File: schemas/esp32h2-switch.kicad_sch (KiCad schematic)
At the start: 19 parts, among them J1 Screw_Terminal_01x02, J2 Screw_Terminal_01x02, K1 SPDT, 5V, 10A 250VAC, Q1 NPN, 40V, 500mA, U1 LM1117MP-3.3, U2 ESP32-H2-DEVKITM-1-N4

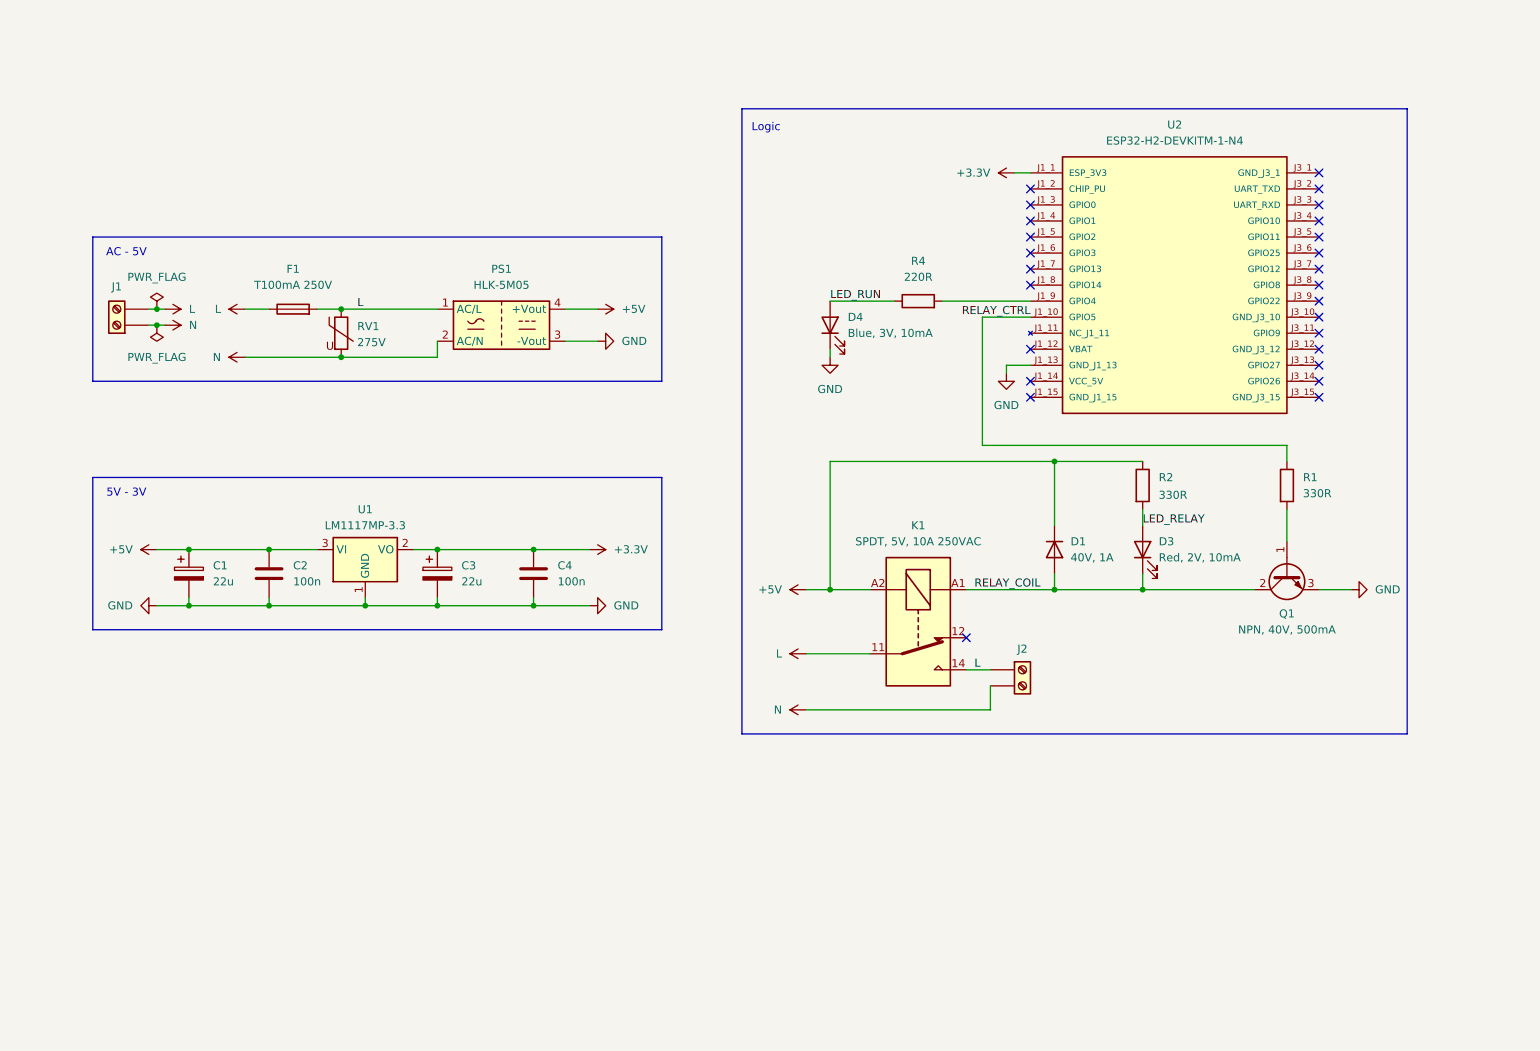
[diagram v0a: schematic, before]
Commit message: Replace devkit on schema with header pings
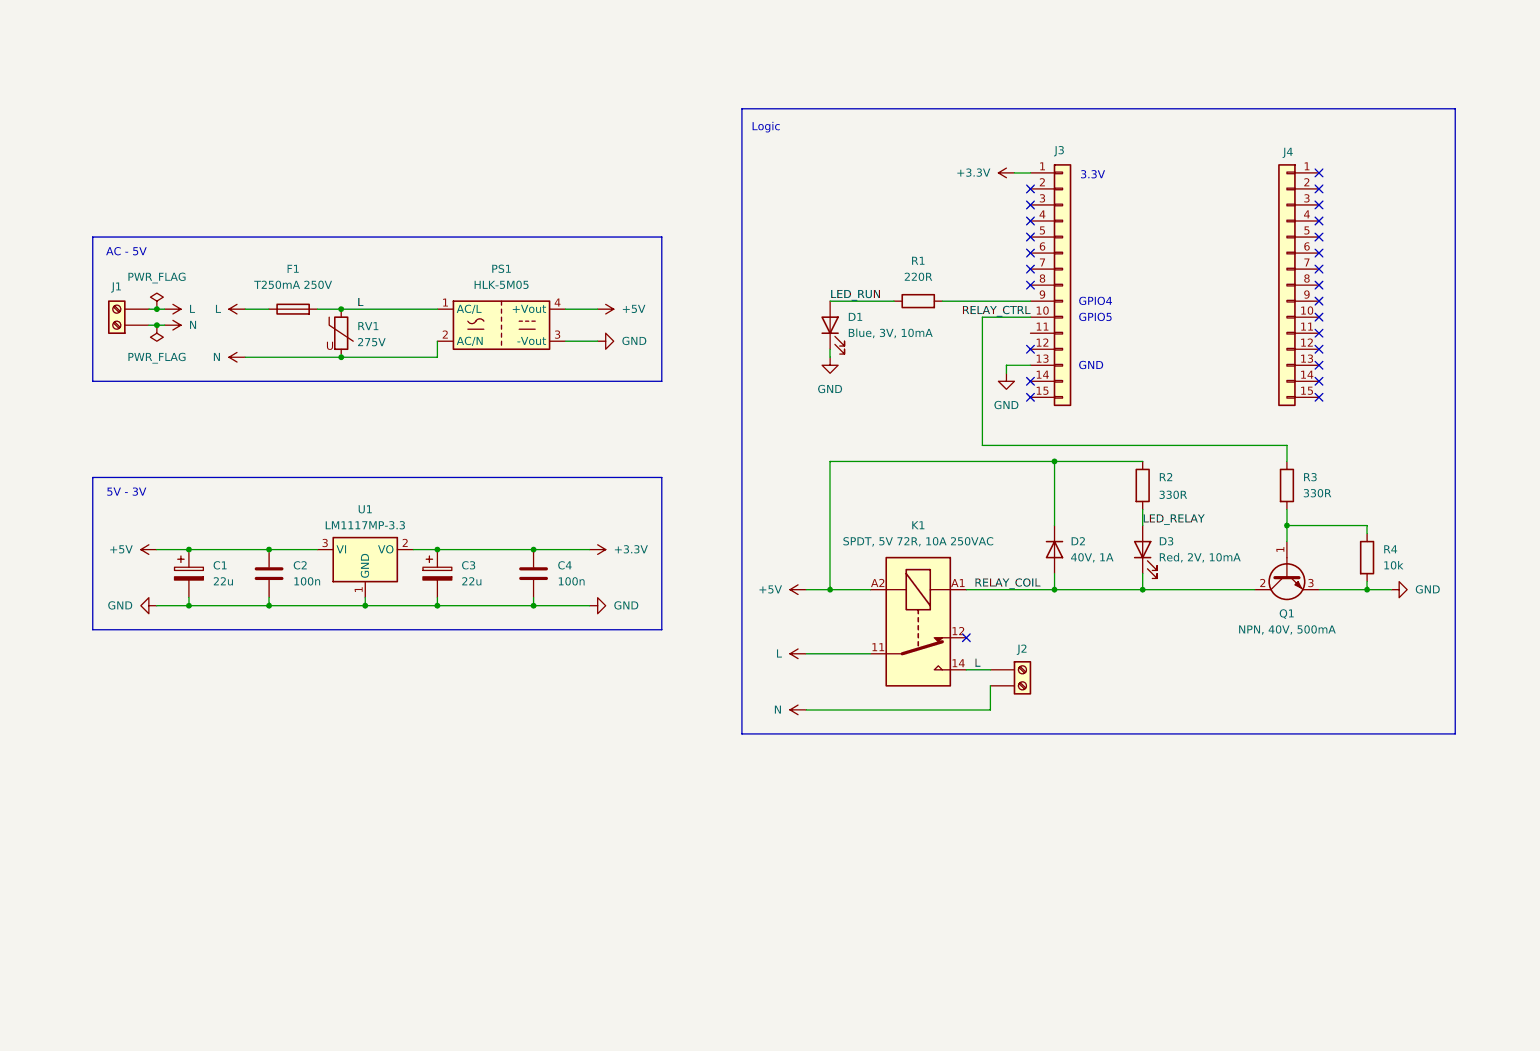
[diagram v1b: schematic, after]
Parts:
- removed U2: ESP32-H2-DEVKITM-1-N4, ESP32-H2-DEVKITM-1-N4:MODULE_ESP32-H2-DEVKITM-1-N4, symbol ESP32-H2-DEVKITM-1-N4:ESP32-H2-DEVKITM-1-N4
- added J3, J4: Conn_01x15, symbol Connector_Generic:Conn_01x15
- added R4: 10k, symbol Device:R
- F1: value T100mA 250V -> T250mA 250V
- K1: value SPDT, 5V, 10A 250VAC -> SPDT, 5V 72R, 10A 250VAC
- renumbered D4 to D1, D1 to D2, R4 to R1, R1 to R3
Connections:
- net +3.3V: now also J3.1 (Pin_1)
- net GND: now also J3.13 (Pin_13), R4.2
- net RELAY_CTRL: now also J3.10 (Pin_10)
- net at Q1.1 (B), R3.2: now also R4.1
- net at R1.2: now also J3.9 (Pin_9)
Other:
- note added: "3.3V"
- note added: "GND"
- note added: "GPIO4"
- note added: "GPIO5"

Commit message: ERC checks
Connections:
- no-connect marks 26 -> 27

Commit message: Add footprints to schematic
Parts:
- C1, C3: footprint (none) -> Sivakov_Capacitors_THT:CP_Radial_D5.0mm_P1.50mm
- C2, C4: footprint (none) -> Capacitor_THT:C_Disc_D5.0mm_W2.5mm_P5.00mm
- D1, D3: footprint (none) -> LED_THT:LED_D3.0mm
- D2: footprint (none) -> Diode_THT:D_DO-41_SOD81_P10.16mm_Horizontal
- F1: footprint (none) -> Sivakov_FuseHolders_THT:FuseHolder_THT_5x20mm_PTF76_RM15mm
- J1, J2: footprint (none) -> TerminalBlock_Phoenix:TerminalBlock_Phoenix_MKDS-1,5-2-5.08_1x02_P5.08mm_Horizontal
- J3, J4: footprint (none) -> Connector_PinSocket_2.54mm:PinSocket_1x15_P2.54mm_Vertical
- K1: footprint (none) -> Sivakov_Relays_THT:Relay_SPDT_Relpol-RM51
- Q1: footprint (none) -> Package_TO_SOT_THT:TO-92_Inline
- R1, R2, R3, R4: footprint (none) -> Resistor_THT:R_Axial_DIN0207_L6.3mm_D2.5mm_P7.62mm_Horizontal
- RV1: footprint (none) -> Varistor:RV_Disc_D9mm_W3.4mm_P5mm
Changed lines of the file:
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@@
 			)
 		)
-		(property "Footprint" ""
+		(property "Footprint" "Package_TO_SOT_THT:TO-92_Inline"
 			(at 231.14 118.11 0)
 			(effects
@@
 			)
 		)
-		(property "Footprint" ""
+		(property "Footprint" "Capacitor_THT:C_Disc_D5.0mm_W2.5mm_P5.00mm"
 			(at 115.2652 116.84 0)
 			(effects
@@
 			)
 		)
-		(property "Footprint" ""
+		(property "Footprint" "TerminalBlock_Phoenix:TerminalBlock_Phoenix_MKDS-1,5-2-5.08_1x02_P5.08mm_Horizontal"
 			(at 191.77 128.27 0)
 			(effects
@@
 			)
 		)
-		(property "Footprint" ""
+		(property "Footprint" "LED_THT:LED_D3.0mm"
 			(at 210.82 109.22 0)
 			(effects
@@
 			)
 		)
-		(property "Footprint" ""
+		(property "Footprint" "Capacitor_THT:C_Disc_D5.0mm_W2.5mm_P5.00mm"
 			(at 73.3552 116.84 0)
 			(effects
@@
 			)
 		)
-		(property "Footprint" ""
+		(property "Footprint" "Diode_THT:D_DO-41_SOD81_P10.16mm_Horizontal"
 			(at 196.85 109.22 0)
 			(effects
@@
 			)
 		)
-		(property "Footprint" ""
+		(property "Footprint" "Resistor_THT:R_Axial_DIN0207_L6.3mm_D2.5mm_P7.62mm_Horizontal"
 			(at 175.26 71.628 90)
 			(effects
@@
 			)
 		)
-		(property "Footprint" ""
+		(property "Footprint" "Sivakov_Relays_THT:Relay_SPDT_Relpol-RM51"
 			(at 173.99 132.08 0)
 			(effects
@@
 			)
 		)
-		(property "Footprint" ""
+		(property "Footprint" "Resistor_THT:R_Axial_DIN0207_L6.3mm_D2.5mm_P7.62mm_Horizontal"
 			(at 209.042 99.06 90)
 			(effects
@@
 			)
 		)
-		(property "Footprint" ""
+		(property "Footprint" "LED_THT:LED_D3.0mm"
 			(at 161.29 73.66 0)
 			(effects
@@
 			)
 		)
-		(property "Footprint" ""
+		(property "Footprint" "Sivakov_Capacitors_THT:CP_Radial_D5.0mm_P1.50mm"
 			(at 100.0252 116.84 0)
 			(effects
@@
 			)
 		)
-		(property "Footprint" ""
+		(property "Footprint" "Varistor:RV_Disc_D9mm_W3.4mm_P5mm"
 			(at 82.042 74.93 90)
 			(effects
@@
 			)
 		)
-		(property "Footprint" ""
+		(property "Footprint" "Sivakov_FuseHolders_THT:FuseHolder_THT_5x20mm_PTF76_RM15mm"
 			(at 76.2 72.898 90)
 			(effects
@@
 			)
 		)
-		(property "Footprint" ""
+		(property "Footprint" "Sivakov_Capacitors_THT:CP_Radial_D5.0mm_P1.50mm"
 			(at 60.6552 116.84 0)
 			(effects
@@
 			)
 		)
-		(property "Footprint" ""
+		(property "Footprint" "Connector_PinSocket_2.54mm:PinSocket_1x15_P2.54mm_Vertical"
 			(at 233.68 67.31 0)
 			(effects
@@
 			)
 		)
-		(property "Footprint" ""
+		(property "Footprint" "TerminalBlock_Phoenix:TerminalBlock_Phoenix_MKDS-1,5-2-5.08_1x02_P5.08mm_Horizontal"
 			(at 48.26 73.66 0)
 			(effects
@@
 			)
 		)
-		(property "Footprint" ""
+		(property "Footprint" "Connector_PinSocket_2.54mm:PinSocket_1x15_P2.54mm_Vertical"
 			(at 198.12 67.31 0)
 			(effects
@@
 			)
 		)
-		(property "Footprint" ""
+		(property "Footprint" "Resistor_THT:R_Axial_DIN0207_L6.3mm_D2.5mm_P7.62mm_Horizontal"
 			(at 244.602 110.49 90)
 			(effects
@@
 			)
 		)
-		(property "Footprint" ""
+		(property "Footprint" "Resistor_THT:R_Axial_DIN0207_L6.3mm_D2.5mm_P7.62mm_Horizontal"
 			(at 231.902 99.06 90)
 			(effects

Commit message: PCB schematic
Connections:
- net L: now also J1.1 (Pin_1); no longer J1.2 (Pin_2)
- net N: now also J1.2 (Pin_2); no longer J1.1 (Pin_1)
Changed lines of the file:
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@@
+	(wire
+		(pts
+			(xy 189.23 80.01) (xy 189.23 81.28)
+		)
+		(stroke
+			(width 0)
+			(type default)
+		)
+	)
 	(wire
 		(pts
@@
 	(wire
 		(pts
-			(xy 189.23 80.01) (xy 189.23 81.28)
-		)
-		(stroke
-			(width 0)
-			(type default)
-		)
-	)
-	(wire
-		(pts
 			(xy 161.29 95.25) (xy 196.85 95.25)
 		)
@@
 	(wire
 		(pts
+			(xy 182.88 128.27) (xy 186.69 128.27)
+		)
+		(stroke
+			(width 0)
+			(type default)
+		)
+	)
+	(wire
+		(pts
 			(xy 196.85 95.25) (xy 196.85 105.41)
 		)
@@
 	(wire
 		(pts
-			(xy 186.69 128.27) (xy 182.88 128.27)
-		)
-		(stroke
-			(width 0)
-			(type default)
-		)
-	)
-	(wire
-		(pts
 			(xy 54.61 73.66) (xy 55.88 73.66)
 		)
@@
 	(wire
 		(pts
+			(xy 186.69 130.81) (xy 186.69 134.62)
+		)
+		(stroke
+			(width 0)
+			(type default)
+		)
+	)
+	(wire
+		(pts
+			(xy 210.82 113.03) (xy 210.82 115.57)
+		)
+		(stroke
+			(width 0)
+			(type default)
+		)
+	)
+	(wire
+		(pts
+			(xy 68.58 78.74) (xy 83.82 78.74)
+		)
+		(stroke
+			(width 0)
+			(type default)
+		)
+	)
+	(wire
+		(pts
+			(xy 161.29 77.47) (xy 161.29 78.74)
+		)
+		(stroke
+			(width 0)
+			(type default)
+		)
+	)
+	(wire
+		(pts
+			(xy 54.61 71.12) (xy 55.88 71.12)
+		)
+		(stroke
+			(width 0)
+			(type default)
+		)
+	)
+	(wire
+		(pts
+			(xy 185.42 72.39) (xy 185.42 92.71)
+		)
+		(stroke
+			(width 0)
+			(type default)
+		)
+	)
+	(wire
+		(pts
+			(xy 59.69 118.11) (xy 72.39 118.11)
+		)
+		(stroke
+			(width 0)
+			(type default)
+		)
+	)
+	(wire
+		(pts
+			(xy 233.68 102.87) (xy 233.68 105.41)
+		)
+		(stroke
+			(width 0)
+			(type default)
+		)
+	)
+	(wire
+		(pts
+			(xy 161.29 95.25) (xy 161.29 115.57)
+		)
+		(stroke
+			(width 0)
+			(type default)
+		)
+	)
+	(wire
+		(pts
+			(xy 54.61 118.11) (xy 59.69 118.11)
+		)
+		(stroke
+			(width 0)
+			(type default)
+		)
+	)
+	(wire
+		(pts
+			(xy 83.82 78.74) (xy 99.06 78.74)
+		)
+		(stroke
+			(width 0)
+			(type default)
+		)
+	)
+	(wire
+		(pts
+			(xy 99.06 118.11) (xy 99.06 116.84)
+		)
+		(stroke
+			(width 0)
+			(type default)
+		)
+	)
+	(wire
+		(pts
+			(xy 161.29 69.85) (xy 171.45 69.85)
+		)
+		(stroke
+			(width 0)
+			(type default)
+		)
+	)
+	(wire
+		(pts
+			(xy 185.42 72.39) (xy 193.04 72.39)
+		)
+		(stroke
+			(width 0)
+			(type default)
+		)
+	)
+	(wire
+		(pts
+			(xy 233.68 105.41) (xy 233.68 107.95)
+		)
+		(stroke
+			(width 0)
+			(type default)
+		)
+	)
+	(wire
+		(pts
 			(xy 53.34 71.12) (xy 54.61 71.12)
-		)
-		(stroke
-			(width 0)
-			(type default)
-		)
-	)
-	(wire
-		(pts
-			(xy 186.69 130.81) (xy 186.69 134.62)
-		)
-		(stroke
-			(width 0)
-			(type default)
-		)
-	)
-	(wire
-		(pts
-			(xy 210.82 113.03) (xy 210.82 115.57)
-		)
-		(stroke
-			(width 0)
-			(type default)
-		)
-	)
-	(wire
-		(pts
-			(xy 68.58 78.74) (xy 83.82 78.74)
-		)
-		(stroke
-			(width 0)
-			(type default)
-		)
-	)
-	(wire
-		(pts
-			(xy 161.29 77.47) (xy 161.29 78.74)
-		)
-		(stroke
-			(width 0)
-			(type default)
-		)
-	)
-	(wire
-		(pts
-			(xy 54.61 71.12) (xy 55.88 71.12)
-		)
-		(stroke
-			(width 0)
-			(type default)
-		)
-	)
-	(wire
-		(pts
-			(xy 185.42 72.39) (xy 185.42 92.71)
-		)
-		(stroke
-			(width 0)
-			(type default)
-		)
-	)
-	(wire
-		(pts
-			(xy 59.69 118.11) (xy 72.39 118.11)
-		)
-		(stroke
-			(width 0)
-			(type default)
-		)
-	)
-	(wire
-		(pts
-			(xy 233.68 102.87) (xy 233.68 105.41)
-		)
-		(stroke
-			(width 0)
-			(type default)
-		)
-	)
-	(wire
-		(pts
-			(xy 161.29 95.25) (xy 161.29 115.57)
-		)
-		(stroke
-			(width 0)
-			(type default)
-		)
-	)
-	(wire
-		(pts
-			(xy 54.61 118.11) (xy 59.69 118.11)
-		)
-		(stroke
-			(width 0)
-			(type default)
-		)
-	)
-	(wire
-		(pts
-			(xy 83.82 78.74) (xy 99.06 78.74)
-		)
-		(stroke
-			(width 0)
-			(type default)
-		)
-	)
-	(wire
-		(pts
-			(xy 99.06 118.11) (xy 99.06 116.84)
-		)
-		(stroke
-			(width 0)
-			(type default)
-		)
-	)
-	(wire
-		(pts
-			(xy 161.29 69.85) (xy 171.45 69.85)
-		)
-		(stroke
-			(width 0)
-			(type default)
-		)
-	)
-	(wire
-		(pts
-			(xy 185.42 72.39) (xy 193.04 72.39)
-		)
-		(stroke
-			(width 0)
-			(type default)
-		)
-	)
-	(wire
-		(pts
-			(xy 233.68 105.41) (xy 233.68 107.95)
 		)
 		(stroke
@@
 		(dnp no)
 		(property "Reference" "J2"
-			(at 191.77 124.968 0)
+			(at 191.77 133.604 0)
 			(effects
 				(font
@@
 	)
 	(symbol
+		(lib_name "R_1")
 		(lib_id "Device:R")
 		(at 175.26 69.85 90)
@@
 	)
 	(symbol
+		(lib_name "R_2")
 		(lib_id "Device:R")
 		(at 210.82 99.06 0)
@@
 	)
 	(symbol
-		(lib_name "Screw_Terminal_01x02_1")
+		(lib_name "Screw_Terminal_01x02_2")
 		(lib_id "Connector:Screw_Terminal_01x02")
-		(at 48.26 73.66 180)
+		(at 48.26 71.12 0)
+		(mirror y)
 		(unit 1)
 		(exclude_from_sim no)
@@
 		(dnp no)
 		(property "Reference" "J1"
-			(at 48.26 67.564 0)
+			(at 48.26 67.818 0)
 			(effects
 				(font
@@
 		)
 		(property "Value" "Screw_Terminal_01x02"
-			(at 48.26 67.31 0)
+			(at 48.26 77.47 0)
 			(effects
 				(font
@@
 		)
 		(property "Footprint" "TerminalBlock_Phoenix:TerminalBlock_Phoenix_MKDS-1,5-2-5.08_1x02_P5.08mm_Horizontal"
-			(at 48.26 73.66 0)
+			(at 48.26 71.12 0)
 			(effects
 				(font
@@
 		)
 		(property "Datasheet" "~"
-			(at 48.26 73.66 0)
+			(at 48.26 71.12 0)
 			(effects
 				(font
@@
 		)
 		(property "Description" "Generic screw terminal, single row, 01x02, script generated (kicad-library-utils/schlib/autogen/connector/)"
-			(at 48.26 73.66 0)
-			(effects
-				(font
+			(at 48.26 71.12 0)
+			(effects
+				(font
